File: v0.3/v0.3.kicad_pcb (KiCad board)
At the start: 4 copper layers, 47.4 x 50.5 mm, 94 parts, among them IC1 M95512-RMN6TP, IC2 TFBS4711-TT1, IC3 BQ25628ERYKR, IC4 RT6150B-33GQW, J1 USB4215-03-A, J2 SWD, J3 BAT, J4 DO0180FMST08, J5 UART, J6 SPEAKER_CONNECTOR, SW1 BUT_R, SW2 BUT_M, SW3 BUT_L, SW4 RUN, SW5 BOOTSEL, U1 RP2350A-QFN60, U2 W25Q128JVP, Y1 ABM8-272-T3, Y2 SIT1533AI-H4-DCC-32.768E

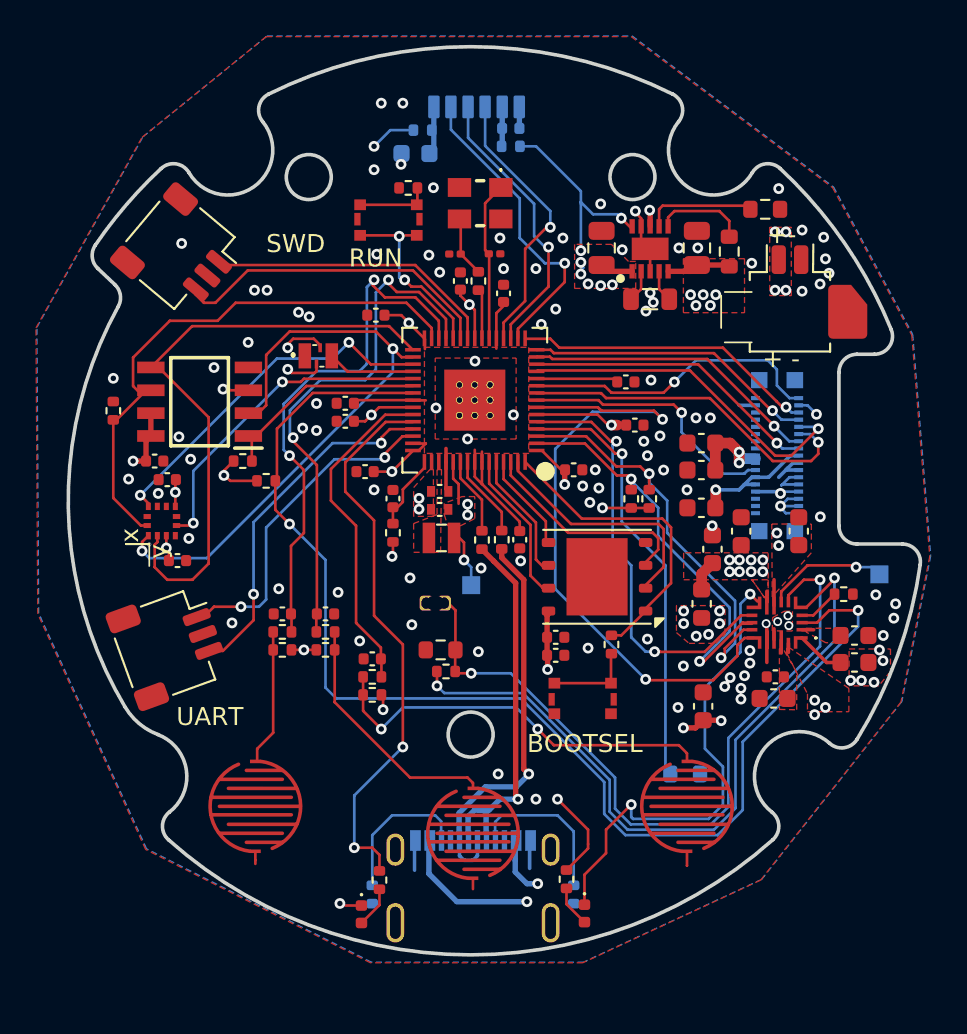
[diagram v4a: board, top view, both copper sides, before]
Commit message: v0.3: small tweaks and added panel tabs
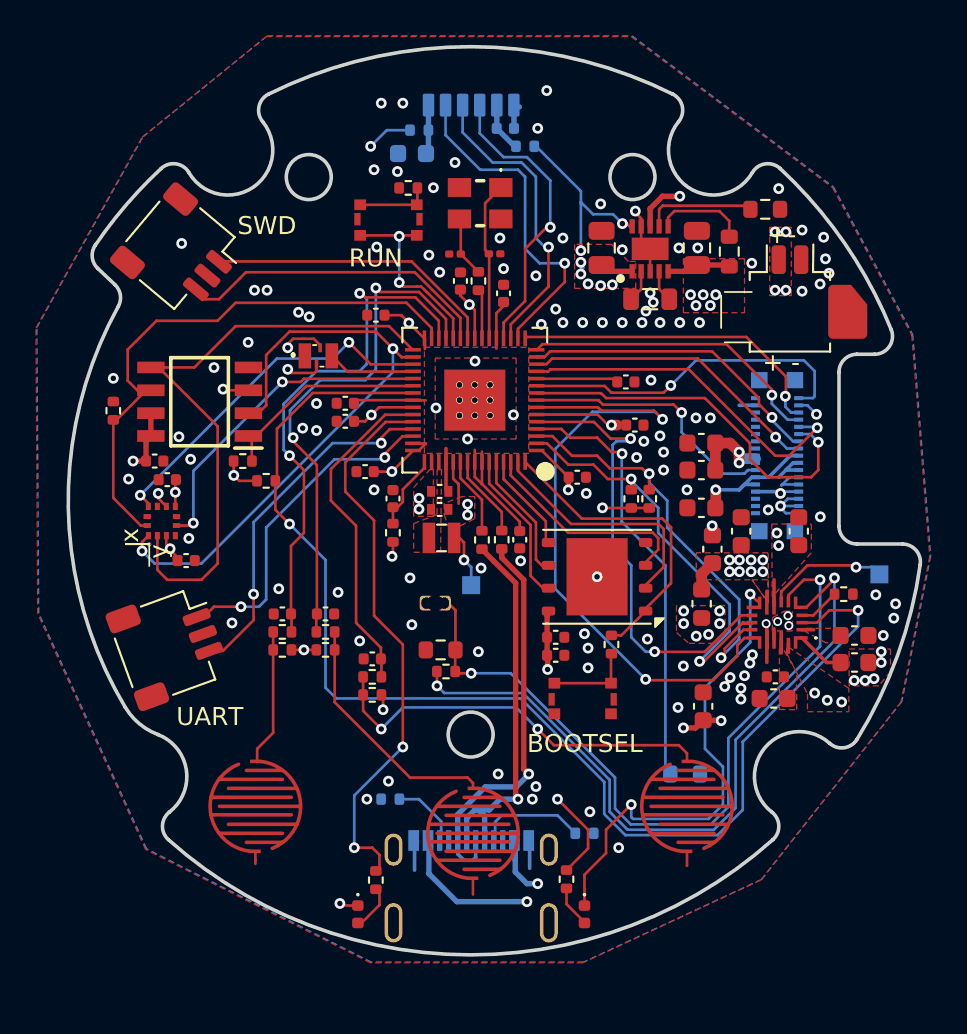
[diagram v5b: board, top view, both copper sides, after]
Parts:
- added REF**: Tab, PCM_kikit:Tab, F.Cu at (140.8, 125.2)
- added REF**: Tab, PCM_kikit:Tab, F.Cu at (140.8, 74.3)
- added REF**: Tab, PCM_kikit:Tab, F.Cu at (118.2, 99.7)
- added REF**: Tab, PCM_kikit:Tab, F.Cu at (164.4, 89.4)
- added REF**: Tab, PCM_kikit:Tab, F.Cu at (165.9, 104.0)
- moved R2 5.39 mm to (136.3, 116.3), turned to 180 degrees
- moved R1 3.45 mm to (147.1, 118.2), turned to 0 degrees
- moved R5 0.80 mm to (143.8, 80.0)
- moved C4 0.48 mm to (125.0, 103.0)
- moved C27 0.46 mm to (146.7, 98.4)
- moved IC2 0.32 mm to (140.8, 77.7)
- moved C2 0.30 mm to (142.7, 79.0)
- moved D1 0.20 mm to (134.5, 122.7)
- moved R34 0.20 mm to (135.5, 120.8)
- moved C3 0.19 mm to (137.5, 80.4)
- moved R6 0.19 mm to (137.9, 79.1)
- moved J1 0.10 mm to (140.8, 118.6)
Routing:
- net /connectors/CC2: track 7.91 -> 3.52 mm
- net /connectors/CC1: track 8.53 -> 5.96 mm
- net VSYS: track 17.8 -> 20.2 mm
- net /mcu/SCREEN_AUX.~{RST}: track 16.9 -> 18.9 mm
- net /mcu/SCREEN_AUX.~{CSB}: track 19.3 -> 21.1 mm
- net /mcu/PWR_AUX.~{BAT_INT}: track 24.2 -> 25.8 mm
- net /irda/IRDA.TX: track 17.2 -> 18.5 mm
- net /mcu/QSPI1.SDIO0: track 16.9 -> 18.0 mm
- net +3.3V: track 81.3 -> 80.3 mm
- net /connectors/USB.D-: track 20.5 -> 21.3 mm
- net /irda/IRDA.RX: track 15.7 -> 16.5 mm
- net /mcu/QSPI1.SDIO1: track 16.2 -> 16.9 mm
- net /accel/SPI.SCK: track 31.3 -> 32.0 mm
- net GND: track 28.6 -> 29.2 mm, vias 95 -> 113
- net /irda/IRDA.SD: track 15.6 -> 16.2 mm
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
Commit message: v0.3: sent to fab
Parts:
- C15, C3, C9: footprint Capacitor_SMD:C_0603_1608Metric -> Capacitor_SMD:C_0402_1005Metric
- SW1, SW2, SW3: footprint CustomFootprints:Button_membrane_5mm -> CustomFootprints:Button_membrane_4.2mm
- moved C9 0.62 mm to (161.5, 108.6)
- moved C15 0.61 mm to (161.5, 107.2)
- moved C3 0.40 mm to (137.9, 80.3)
- moved C28 0.20 mm to (142.8, 88.2)
- moved C37 0.20 mm to (142.3, 86.0)
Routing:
- net GND: track 29.2 -> 30.4 mm, vias 113 -> 128
- net Net-(IC2-VCC2/IRED/ANODE): track 2.70 -> 2.15 mm
- net /buttons/BUT_L_1: track 7.47 -> 8.01 mm
- net /buttons/BUT_M_1: track 13.7 -> 14.2 mm
- net /connectors/BAT+: vias 6 -> 8
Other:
- board text added: "D"
- board text added: "K"
- board text added: "RX"
- board text added: "TX"
